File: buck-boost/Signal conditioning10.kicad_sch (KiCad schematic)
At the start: 16 parts, among them U11 Opamp_Dual, U13 Opamp_Dual

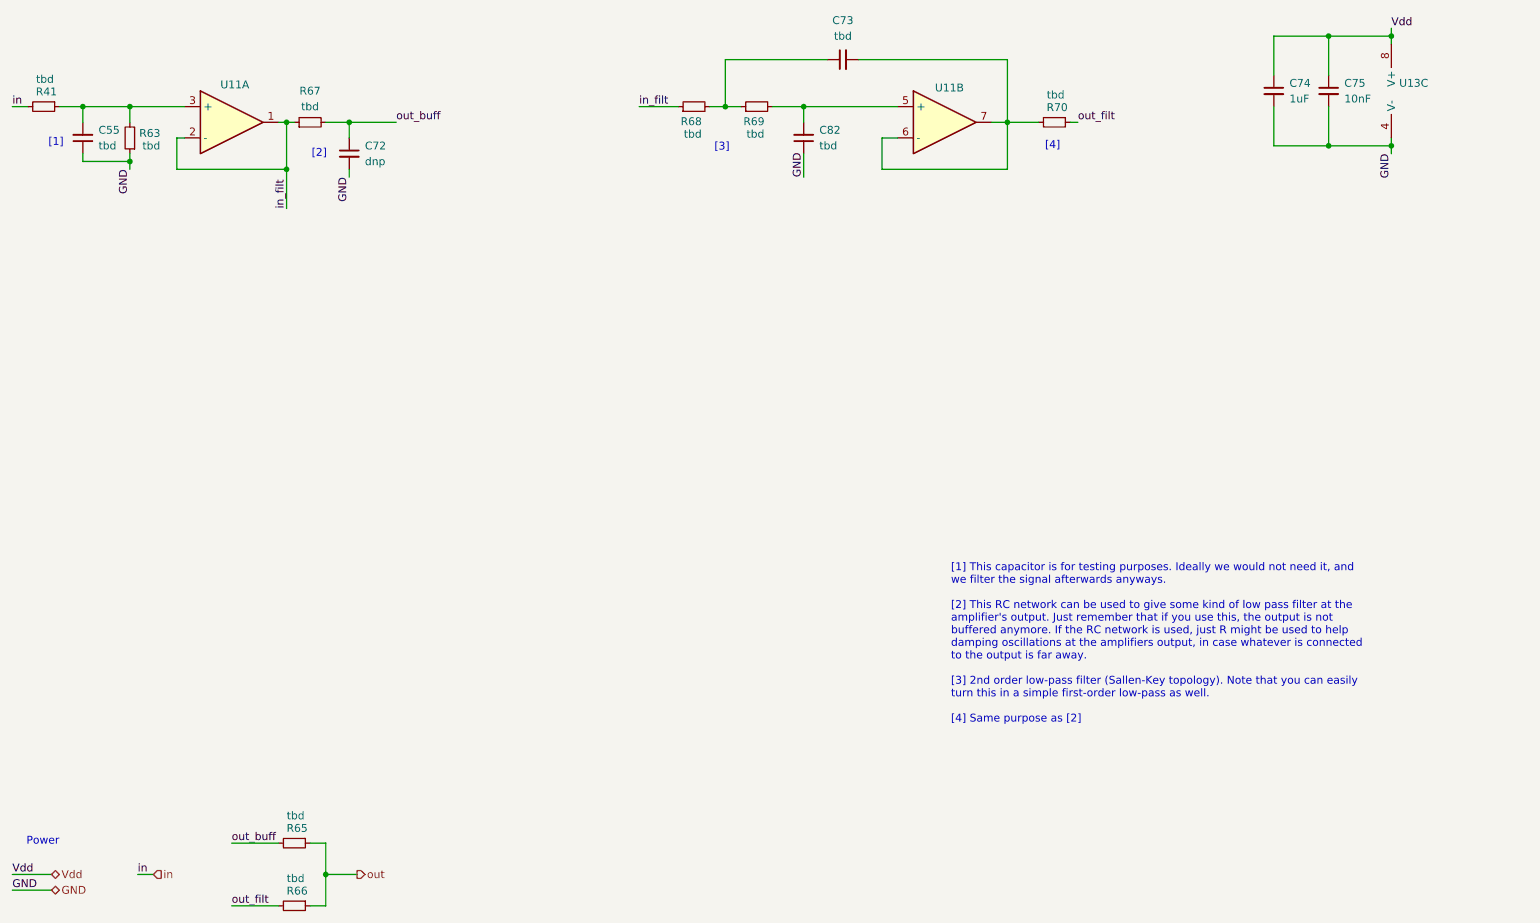
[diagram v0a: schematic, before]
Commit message: Editing sheets(Power labels, sheet color, adding text), Adding information in the sensor sheets
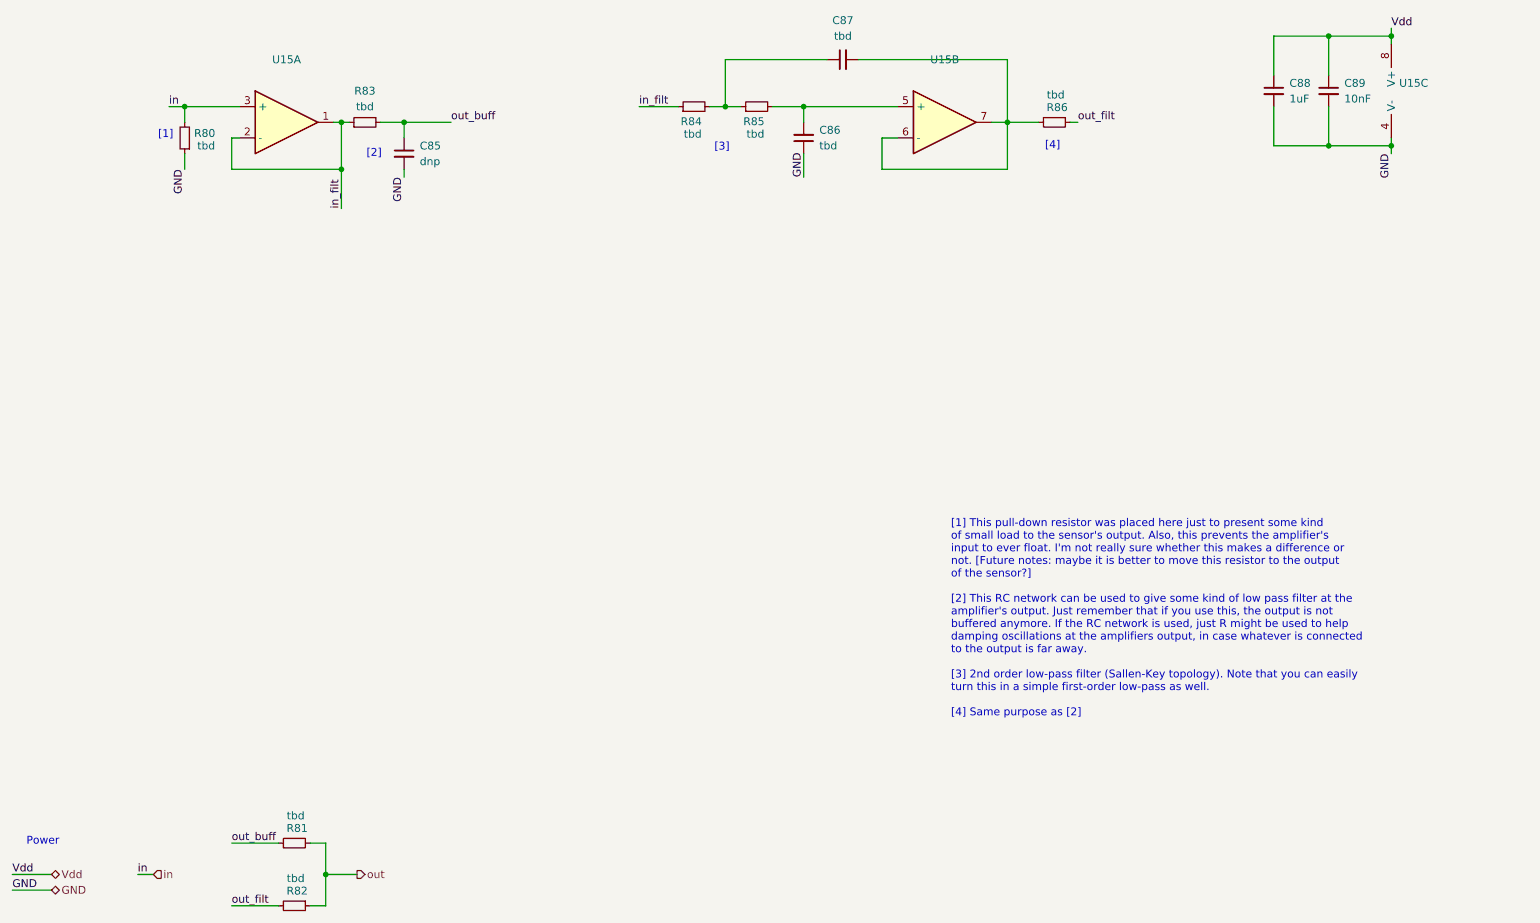
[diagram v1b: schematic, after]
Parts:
- removed C55: tbd, Capacitor_SMD:C_0805_2012Metric_Pad1.18x1.45mm_HandSolder, symbol Device:C_Small
- removed R41: tbd, Resistor_SMD:R_0805_2012Metric_Pad1.20x1.40mm_HandSolder, symbol Device:R_Small
- removed U11, U13: Opamp_Dual, symbol Device:Opamp_Dual
- added U15: Opamp_Dual, symbol Device:Opamp_Dual
- renumbered C72 to C85, C82 to C86, C73 to C87, C74 to C88, C75 to C89, R63 to R80, R65 to R81, R66 to R82, R67 to R83, R68 to R84, R69 to R85, R70 to R86
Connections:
- net GND: now also U15.4 (V-)
- net Vdd: now also U15.8 (V+)
- net in: now also R80.2, U15.3 (+)
- net in_filt: now also U15.1, U15.2 (-)
- net at C86.2, R85.2: now also U15.5 (+)
- net at C87.2, R86.2: now also U15.6 (-), U15.7
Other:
- note added: "[1] This pull-down resistor was placed here just to present some kind of small load to the sensor's output. Also, this prevents the amplifier's input to ever float. I'm not really sure whether this makes a difference or not. [Future notes: maybe it is better to move this resistor to the output of the sensor?] [2] This RC network can be used to give some kind of low pass filter at the amplifier's 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"
- note removed: "[1] This capacitor is for testing purposes. Ideally we would not need it, and we filter the signal afterwards anyways. [2] This RC network can be used to give some kind of low pass filter at the amplifier's output. Just remember that if you use this, the output is not buffered anymore. If the RC network is used, just R might be used to help damping oscillations at the amplifiers output, in case w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"
- moved on the sheet: C85, R80, R83

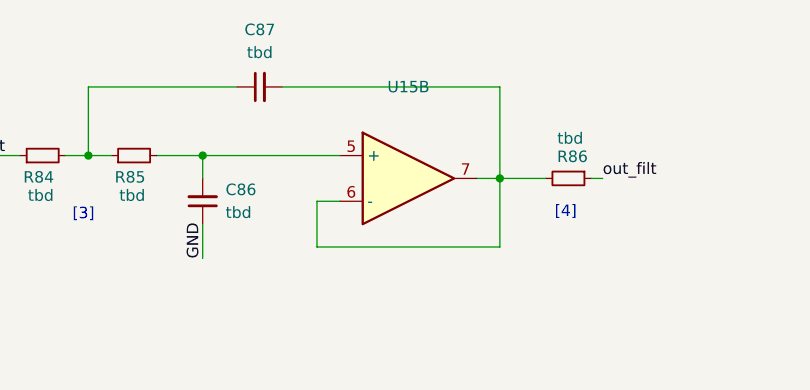
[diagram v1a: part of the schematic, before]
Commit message: Adding supply block
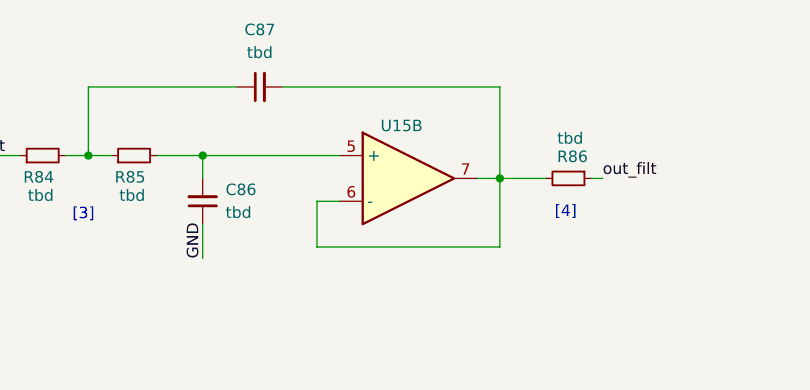
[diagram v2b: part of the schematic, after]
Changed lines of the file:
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@@
 		(on_board yes)
 		(dnp no)
-		(fields_autoplaced yes)
 		(property "Reference" "U15"
-			(at 176.53 45.72 0)
+			(at 175.768 50.038 0)
 			(effects
 				(font
